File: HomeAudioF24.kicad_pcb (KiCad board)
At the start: 4 copper layers, 214 x 114 mm, 26 parts, among them U1 LF356M, U2 LF356M, U3 LF356M, U4 LF356M, U5 LF356M, U6 LF356M, U7 LF356M

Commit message: First Major Revision
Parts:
- added Brd1: SSD1306, Display_New:128x64OLED SSD1306, F.Cu at (215.5, 142.6)
- added C10: 47nF, ColorOrgan:C_Disc_D4.3mm_W1.9mm_P5.00mm_Handsolder, F.Cu at (116.5, 177.0)
- added C11: 47nF, ColorOrgan:C_Disc_D4.3mm_W1.9mm_P5.00mm_Handsolder, F.Cu at (107.1, 187.0)
- added C12: 470nF, ColorOrgan:R_Combo, F.Cu at (59.5, 209.0)
- added C13: 470nF, ColorOrgan:R_Combo, F.Cu at (59.5, 233.0)
- added C14: 1μF, ColorOrgan:C_Disc_D4.3mm_W1.9mm_P5.00mm_Handsolder, F.Cu at (133.5, 228.0)
- added C15: 1μF, ColorOrgan:C_Disc_D4.3mm_W1.9mm_P5.00mm_Handsolder, F.Cu at (133.5, 216.0)
- added C16: 2.2nF, ColorOrgan:C_Disc_D4.3mm_W1.9mm_P5.00mm_Handsolder, F.Cu at (190.5, 42.0)
- added C17: 2.2nF, ColorOrgan:C_Disc_D4.3mm_W1.9mm_P5.00mm_Handsolder, F.Cu at (193.0, 77.4)
- added C18: 22nF, ColorOrgan:C_Disc_D4.3mm_W1.9mm_P5.00mm_Handsolder, F.Cu at (182.0, 104.9)
- added C19: 22nF, ColorOrgan:C_Disc_D4.3mm_W1.9mm_P5.00mm_Handsolder, F.Cu at (189.5, 105.0)
- added C20: 100nF, ColorOrgan:C_Disc_D4.3mm_W1.9mm_P5.00mm_Handsolder, F.Cu at (197.5, 105.0)
- added C21: 10nF, ColorOrgan:C_Disc_D4.3mm_W1.9mm_P5.00mm_Handsolder, F.Cu at (194.6, 118.0)
- added C22: 10nF, ColorOrgan:C_Disc_D4.3mm_W1.9mm_P5.00mm_Handsolder, F.Cu at (192.5, 182.0)
- added C23: 10nF, ColorOrgan:C_Disc_D4.3mm_W1.9mm_P5.00mm_Handsolder, F.Cu at (207.5, 182.0)
- added C24: 10nF, ColorOrgan:C_Disc_D4.3mm_W1.9mm_P5.00mm_Handsolder, F.Cu at (222.5, 182.0)
- added C25: 100nF, ColorOrgan:C_Disc_D4.3mm_W1.9mm_P5.00mm_Handsolder, F.Cu at (47.0, 34.0)
- added C7: 22nF, ColorOrgan:C_Disc_D4.3mm_W1.9mm_P5.00mm_Handsolder, F.Cu at (59.5, 193.0)
- added C8: 4.7nF, ColorOrgan:C_Disc_D4.3mm_W1.9mm_P5.00mm_Handsolder, F.Cu at (83.5, 177.0)
- added C9: 47nF, ColorOrgan:C_Disc_D4.3mm_W1.9mm_P5.00mm_Handsolder, F.Cu at (125.5, 187.0)
- added D1: 1N4001, Diode_THT:D_DO-41_SOD81_P10.16mm_Horizontal, F.Cu at (184.6, 59.0)
- added D2: 1N4001, Diode_THT:D_DO-41_SOD81_P10.16mm_Horizontal, F.Cu at (174.4, 66.0)
- added D3: 1N5817, Diode_THT:D_DO-41_SOD81_P10.16mm_Horizontal, F.Cu at (192.1, 128.0)
- added D4: 1N4001, Diode_THT:D_DO-41_SOD81_P10.16mm_Horizontal, F.Cu at (192.4, 198.7)
- added D5: 1N4001, Diode_THT:D_DO-41_SOD81_P10.16mm_Horizontal, F.Cu at (207.7, 198.9)
- added D6: 1N4001, Diode_THT:D_DO-41_SOD81_P10.16mm_Horizontal, F.Cu at (222.5, 198.9)
- added G***: LOGO, 4PinButton:vtSilkscreenFootPrint, F.Cu at (209.2, 223.2)
- added J1: AudioJack2_Ground, ColorOrgan:Jack_3.5mm_Ground_RightAngle, F.Cu at (225.5, 83.0)
- added J2: AD2 Connections, Connector_PinHeader_2.54mm:PinHeader_1x06_P2.54mm_Vertical, F.Cu at (27.5, 42.4)
- added J3: Ardunio Conections, Connector_PinHeader_2.54mm:PinHeader_1x08_P2.54mm_Vertical, F.Cu at (27.5, 63.4)
- added JP1: SolderJumper_2_Open, Jumper:SolderJumper-2_P1.3mm_Open_TrianglePad1.0x1.5mm, F.Cu at (184.8, 118.0)
- added JP2: SolderJumper_2_Open, Jumper:SolderJumper-2_P1.3mm_Open_TrianglePad1.0x1.5mm, F.Cu at (38.3, 34.0)
- added JP3: SolderJumper_2_Open, Jumper:SolderJumper-2_P1.3mm_Open_TrianglePad1.0x1.5mm, F.Cu at (62.8, 34.0)
- added L1: ≈702.37μH, ColorOrgan:InductorCore, F.Cu at (149.5, 103.0)
- added Q1: 2N7000, Package_TO_SOT_THT:TO-92_Inline, F.Cu at (203.5, 72.5)
- added Q2: TP0606, Package_TO_SOT_THT:TO-92L_Inline, F.Cu at (203.5, 49.4)
- added R14: 4.7k, ColorOrgan:1_2W Res + 1206, F.Cu at (41.5, 177.0)
- added R15: 6.8k, ColorOrgan:1_2W Res + 1206, F.Cu at (59.5, 176.0)
- added R16: 3.3k, ColorOrgan:1_2W Res + 1206, F.Cu at (72.5, 186.0)
- added R17: 4.7k, ColorOrgan:1_2W Res + 1206, F.Cu at (116.5, 198.0)
- added R18: 22k, ColorOrgan:1_2W Res + 1206, F.Cu at (135.5, 177.0)
- added R19: 820, ColorOrgan:1_2W Res + 1206, F.Cu at (41.5, 215.0)
- added R20: 820, ColorOrgan:1_2W Res + 1206, F.Cu at (72.5, 215.0)
- added R21: 68k, ColorOrgan:1_2W Res + 1206, F.Cu at (99.5, 226.0)
- added R22: 82k, ColorOrgan:1_2W Res + 1206, F.Cu at (99.5, 244.0)
- added R23: 1.8k, ColorOrgan:1_2W Res + 1206, F.Cu at (113.5, 214.4)
- added R24: 1.5k, ColorOrgan:1_2W Res + 1206, F.Cu at (147.5, 222.0)
- added R25: 150k, ColorOrgan:1_2W Res + 1206, F.Cu at (173.5, 227.0)
- added R26: 180k, ColorOrgan:1_2W Res + 1206, F.Cu at (173.5, 245.0)
- added R27: 330, ColorOrgan:1_2W Res + 1206, F.Cu at (131.5, 49.0)
- added R28: 2.2k, ColorOrgan:1_2W Res + 1206, F.Cu at (144.5, 55.0)
- added R29: 100, ColorOrgan:1_2W Res + 1206, F.Cu at (179.5, 52.0)
- added R30: 100, ColorOrgan:1_2W Res + 1206, F.Cu at (178.5, 72.0)
- added R31: 56, ColorOrgan:1_2W Res + 1206, F.Cu at (229.5, 56.0)
- added R32: 68, ColorOrgan:1_2W Res + 1206, F.Cu at (223.4, 56.0)
- added R33: 39k, ColorOrgan:1_2W Res + 1206, F.Cu at (158.0, 127.5)
- added R34: 100k, ColorOrgan:1_2W Res + 1206, F.Cu at (158.0, 133.6)
- added R35: 82k, ColorOrgan:1_2W Res + 1206, F.Cu at (183.5, 166.0)
- added R36: 2.2k, ColorOrgan:1_2W Res + 1206, F.Cu at (94.5, 99.0)
- added RV1: R_Potentiometer, Potentiometer_THT:Potentiometer_Vishay_148-149_Single_Vertical, F.Cu at (81.4, 40.5)
- added RV2: R_Potentiometer, Potentiometer_THT:Potentiometer_Vishay_148-149_Single_Vertical, F.Cu at (81.4, 59.5)
- added RV3: R_Potentiometer, Potentiometer_THT:Potentiometer_Vishay_148-149_Single_Vertical, F.Cu at (81.4, 79.5)
- added S1: VS-1213-67-160GF, 4PinButton:SW_VS-1213-67-160GF, F.Cu at (181.3, 143.5)
- added TP1: Treble_Test, TestPoint:TestPoint_Pad_2.5x2.5mm, F.Cu at (153.5, 147.0)
- added TP2: Mid_Test, TestPoint:TestPoint_Pad_2.5x2.5mm, F.Cu at (159.5, 189.0)
- added TP3: Bass Test, TestPoint:TestPoint_Pad_2.5x2.5mm, F.Cu at (173.5, 216.0)
- added TP4: Modulator_test, TestPoint:TestPoint_Pad_2.5x2.5mm, F.Cu at (119.5, 110.0)
- added TP5: SquareWave_Test, TestPoint:TestPoint_Pad_2.5x2.5mm, F.Cu at (169.5, 43.0)
- added TP6: FinalWave_Test, TestPoint:TestPoint_Pad_2.5x2.5mm, F.Cu at (210.5, 106.0)
- added TP7: A0_Test, TestPoint:TestPoint_Pad_2.5x2.5mm, F.Cu at (199.5, 192.0)
- added TP8: A1_Test, TestPoint:TestPoint_Pad_2.5x2.5mm, F.Cu at (213.5, 192.0)
- added TP9: A2_Test, TestPoint:TestPoint_Pad_2.5x2.5mm, F.Cu at (227.5, 192.0)
- added U10: LF356M, Package_DIP:DIP-8_W7.62mm_LongPads, F.Cu at (82.7, 215.2)
- added U11: LF356M, Package_DIP:DIP-8_W7.62mm_LongPads, F.Cu at (156.7, 215.2)
- added U12: LF356M, Package_DIP:DIP-8_W7.62mm_LongPads, F.Cu at (157.5, 54.4)
- added U8: LF356M, Package_DIP:DIP-8_W7.62mm_LongPads, F.Cu at (88.7, 183.2)
- added U9: LF356M, Package_DIP:DIP-8_W7.62mm_LongPads, F.Cu at (142.7, 183.2)
- C1: value .01μ -> 10nF; footprint ColorOrgan:R_Combo -> ColorOrgan:C_Disc_D4.3mm_W1.9mm_P5.00mm_Handsolder
- C2: value .1μ -> 100nF; footprint ColorOrgan:R_Combo -> ColorOrgan:C_Disc_D4.3mm_W1.9mm_P5.00mm_Handsolder
- C3, C4, C5, C6: footprint ColorOrgan:R_Combo -> ColorOrgan:C_Disc_D4.3mm_W1.9mm_P5.00mm_Handsolder
- moved R8 130.9 mm to (42.5, 143.0)
- moved R9 126.7 mm to (53.5, 157.0), turned to 90 degrees
- moved C3 109.7 mm to (64.5, 145.7)
- moved R4 105.5 mm to (42.5, 42.0)
- moved R10 105.5 mm to (76.5, 157.0), turned to -90 degrees
- moved C4 98.9 mm to (64.5, 137.0)
- moved R5 93.9 mm to (59.5, 42.0)
- moved R6 80.7 mm to (64.5, 66.0)
- moved U4 78.8 mm to (54.9, 48.4)
- moved C5 75.6 mm to (117.1, 149.0)
- moved R12 74.3 mm to (107.5, 155.0), turned to 90 degrees
- moved R11 73.6 mm to (101.5, 143.0)
- moved U5 67.9 mm to (105.7, 54.2)
- moved R13 58.9 mm to (127.5, 155.0), turned to -90 degrees
- moved C6 57.3 mm to (117.1, 136.0)
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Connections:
- R3 pad 1: Net-(U1-OUT) -> Net-(U3--IN)
- U3 pad 2: Net-(U1-OUT) -> Net-(U3--IN)
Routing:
- net A1: track 0.00 -> 401.2 mm, vias 0 -> 2
- net A0: track 0.00 -> 399.8 mm, vias 0 -> 2
- net A2: track 0.00 -> 399.8 mm
- net Bass_Out: track 0.00 -> 303.8 mm, vias 0 -> 2
- net Treble_Out: track 0.00 -> 302.0 mm, vias 0 -> 2
- net Mid_Out: track 0.00 -> 299.1 mm, vias 0 -> 2
- net SDA: track 0.00 -> 239.8 mm, vias 0 -> 4
- net Bass_In: track 0.00 -> 233.9 mm, vias 0 -> 2
- net SCL: track 0.00 -> 218.4 mm
- net Button_Pin: track 0.00 -> 180.5 mm, vias 0 -> 2
- net Net-(U5--IN): track 0.00 -> 177.3 mm
- net Net-(JP1-A): track 0.00 -> 123.7 mm
- net Net-(U4--IN): track 0.00 -> 110.1 mm
- net Net-(Q1-D): track 0.00 -> 85.1 mm
- net Modulator_Out: track 0.00 -> 84.5 mm
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- added copper zone on In2.Cu, net +3.3V
- added copper zone on In2.Cu, net -5V
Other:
- board size 214 x 114 mm -> 220 x 236 mm
- board text added: "+3.3V"
- board text added: "+5V"
- board text added: "-5V"
- board text added: "A0"
- board text added: "A1"
- board text added: "A2"
- board text added: "Audio"
- board text added: "Bass"
- board text added: "By Shane Wyman &"
- board text added: "Colin Edsall"
- board text added: "Comparator And Switching Stage"
- board text added: "Equalizer"
- board text added: "Fall 2024"
- board text added: "GND"
- board text added: "Home Audio System"
- board text added: "I hope they play FEIN"
- board text added: "Mid"
- board text added: "Modulator"
- board text added: "Pin 3"
- board text added: "Pin 8"
- board text added: "RTX Enabled"
- board text added: "SCL"
- board text added: "SDA"
- board text added: "Treble"

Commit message: Compact version done
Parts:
- RV1: value R_Potentiometer -> Treble
- RV2: value R_Potentiometer -> Mid
- RV3: value R_Potentiometer -> Bass
- moved TP9 193.4 mm to (55.5, 103.5)
- moved C24 192.3 mm to (44.5, 109.2), turned to 0 degrees
- moved D6 190.7 mm to (54.2, 109.2), turned to 0 degrees
- moved R19 189.3 mm to (181.5, 87.5)
- moved C13 185.5 mm to (196.8, 108.2)
- moved R22 182.7 mm to (203.5, 93.8), turned to 0 degrees
- moved R21 179.2 mm to (213.2, 87.5), turned to 0 degrees
- moved R20 178.5 mm to (197.5, 87.5), turned to 0 degrees
- moved TP8 161.0 mm to (79.0, 103.5)
- moved C12 159.4 mm to (183.1, 108.2)
- moved U10 159.1 mm to (185.2, 93.5)
- moved G*** 158.8 mm to (155.8, 73.8)
- moved C14 158.5 mm to (228.0, 100.8)
- moved R24 157.2 mm to (229.0, 87.5), turned to 0 degrees
- moved S1 156.7 mm to (31.5, 97.5), turned to 0 degrees
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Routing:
- net A2: track 399.8 -> 66.7 mm
- net A1: track 401.2 -> 99.6 mm, vias 2 -> 0
- net A0: track 399.8 -> 129.6 mm, vias 2 -> 0
- net Treble_Out: track 302.0 -> 126.7 mm, vias 2 -> 0
- net Mid_Out: track 299.1 -> 131.9 mm, vias 2 -> 1
- net Button_Pin: track 180.5 -> 24.5 mm, vias 2 -> 1
- net Bass_Out: track 303.8 -> 229.2 mm, vias 2 -> 0
- net Net-(U5--IN): track 177.3 -> 113.6 mm
- net Net-(Q1-D): track 85.1 -> 34.4 mm
- net Net-(U11--IN): track 24.8 -> 65.2 mm
- net Net-(C5-Pad1): track 37.1 -> 75.4 mm
- net Net-(D1-A): track 51.0 -> 87.7 mm
- net Modulator_Out: track 84.5 -> 48.9 mm, vias 0 -> 1
- net Net-(U4--IN): track 110.1 -> 142.5 mm
- net Net-(C7-Pad1): track 47.3 -> 76.4 mm
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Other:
- board size 220 x 236 mm -> 220 x 90.8 mm
- board text added: "By Shane Wyman & Colin Edsall"
- board text added: "Press Button To Start"
- board text removed: "Bass"
- board text removed: "By Shane Wyman &"
- board text removed: "Colin Edsall"
- board text removed: "Comparator And Switching Stage"
- board text removed: "Equalizer"
- board text removed: "Mid"
- board text removed: "Modulator"
- board text removed: "RTX Enabled"
- board text removed: "Treble"

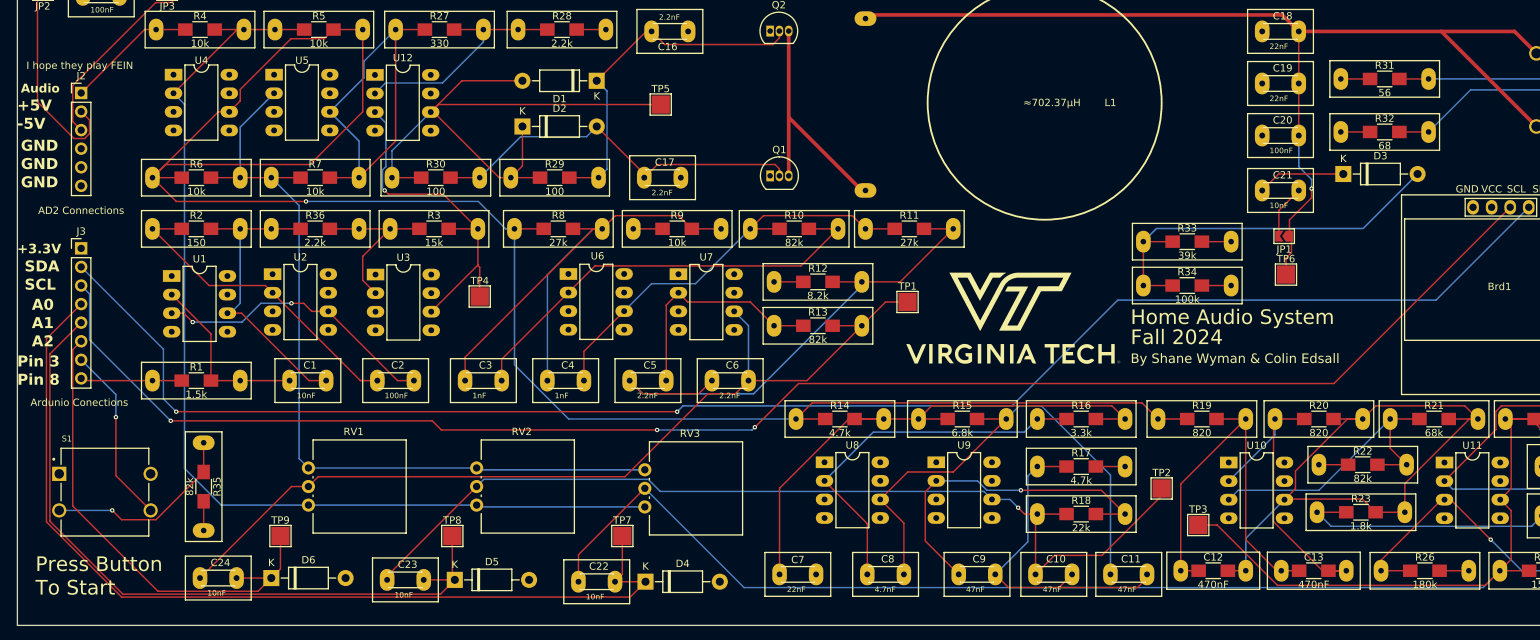
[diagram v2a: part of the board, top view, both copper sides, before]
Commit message: Fixed some silkscreens
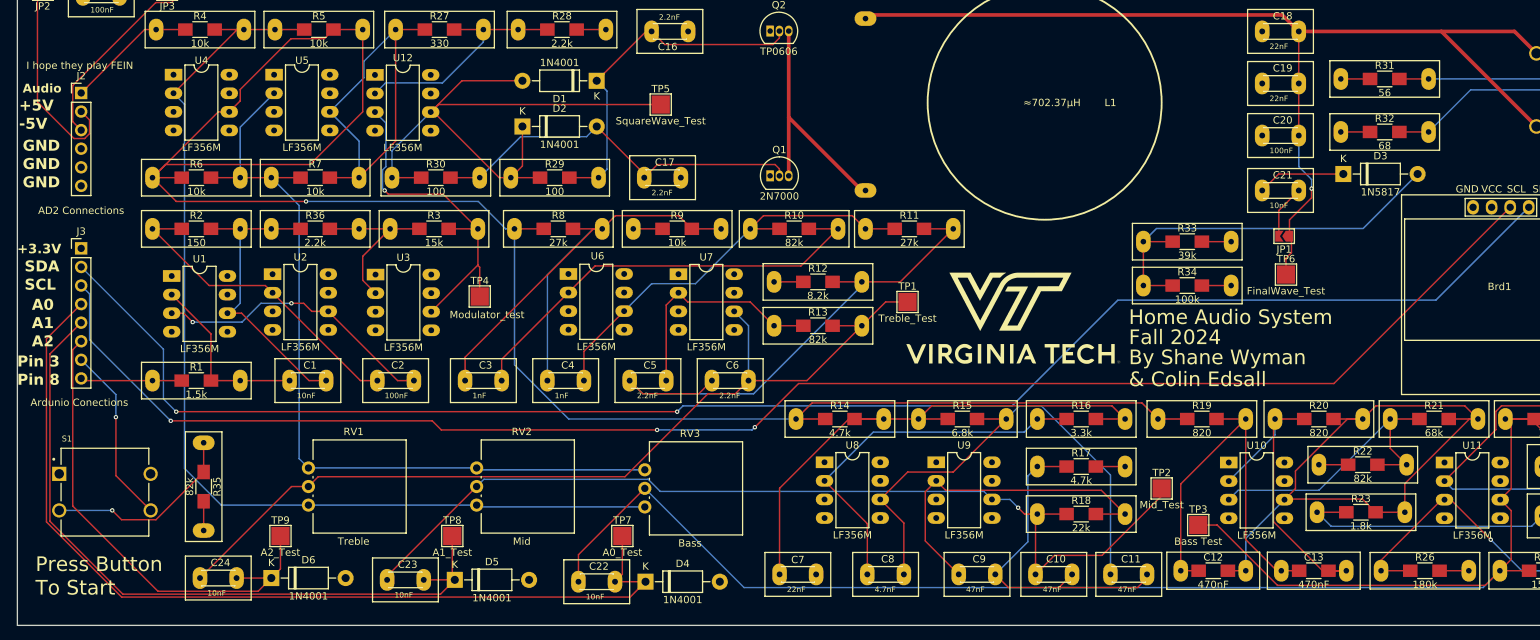
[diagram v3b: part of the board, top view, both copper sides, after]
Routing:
- net Net-(U9--IN): vias 1 -> 0
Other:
- board text added: "& Colin Edsall"
- board text added: "By Shane Wyman"
- board text removed: "By Shane Wyman & Colin Edsall"
